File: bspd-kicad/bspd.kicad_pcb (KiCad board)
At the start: 2 copper layers, 100 x 80 mm, 113 parts, among them Q1 AO3400A, Q2 AO3401A, SW1 CJS-1200TB1, SW2 CJS-1200TB1, U5 SN74HC74DR, U6 LM1117MP-5.0, U7 SN74LVC2G14DBVR, U8 SN74LVC3G14DCUR, U9 SN74LVC3G14DCUR

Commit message: Layout Progress
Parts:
- added J1: BSPD Connector, bspd:MOLEX_430450800, F.Cu at (32.1, 125.3)
- moved C11 115.7 mm to (63.5, 141.5)
- moved R24 115.7 mm to (66.5, 139.2)
- moved R28 115.7 mm to (66.5, 143.5)
- moved TP7 115.7 mm to (66.2, 134.8)
- moved C10 115.6 mm to (57.0, 141.5)
- moved R23 115.6 mm to (60.0, 139.2)
- moved R27 115.6 mm to (60.0, 143.5)
- moved TP6 115.6 mm to (60.0, 135.0)
- moved C9 115.6 mm to (50.5, 141.2)
- moved R22 115.6 mm to (53.5, 139.2)
- moved R26 115.6 mm to (53.5, 143.5)
- moved TP5 115.6 mm to (54.0, 134.8)
- moved C8 115.5 mm to (44.0, 141.2)
- moved R21 115.5 mm to (47.0, 139.2)
- moved R25 115.5 mm to (47.0, 143.5)
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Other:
- board size 100 x 80 mm -> 79.5 x 60.8 mm
- copper layers 2 -> 4
- board text added: "FLT"
- board text added: "HB"
- board text added: "LATCH"
- board text added: "TP1"
- board text added: "TP2"
- board text added: "TPx10"

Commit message: Draft complete
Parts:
- added H1: MountingHole_Pad, MountingHole:MountingHole_3.2mm_M3_ISO14580_Pad, F.Cu at (95.0, 97.0)
- added H2: MountingHole_Pad, MountingHole:MountingHole_3.2mm_M3_ISO14580_Pad, F.Cu at (27.5, 151.0)
- added H3: MountingHole_Pad, MountingHole:MountingHole_3.2mm_M3_ISO14580_Pad, F.Cu at (27.5, 97.0)
- added H4: MountingHole_Pad, MountingHole:MountingHole_3.2mm_M3_ISO14580_Pad, F.Cu at (95.0, 151.0)
- J1: footprint bspd:MOLEX_430450800 -> bspd:MOLEX_430450600
- R29: value 47k -> 49.9k
- R30: value 56k -> 54.9k
- moved R39 15.1 mm to (44.0, 151.5), turned to 180 degrees
- moved D10 13.6 mm to (35.0, 153.5), turned to 180 degrees
- moved R11 13.5 mm to (86.0, 110.4), turned to 90 degrees
- moved R41 11.5 mm to (44.0, 149.5), turned to 180 degrees
- moved D9 11.0 mm to (48.5, 151.5), turned to 0 degrees
- moved D13 10.5 mm to (35.0, 151.5), turned to 180 degrees
- moved R40 9.63 mm to (39.5, 153.5), turned to 0 degrees
- moved D11 8.75 mm to (48.5, 149.5), turned to 0 degrees
- moved R42 8.41 mm to (44.0, 147.5), turned to 180 degrees
- moved D14 8.36 mm to (35.0, 149.5), turned to 180 degrees
- moved C16 8.28 mm to (35.5, 135.5), turned to 180 degrees
- moved D12 8.05 mm to (48.5, 147.5), turned to 0 degrees
- moved D15 7.76 mm to (35.0, 147.5), turned to 180 degrees
- moved U6 7.16 mm to (30.0, 136.0), turned to 90 degrees
- moved D5 5.88 mm to (30.0, 143.0), turned to 180 degrees
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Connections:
- R30 pad 1: Net-(Q2-G) -> +12V
- R30 pad 2: +12V -> Net-(Q2-G)
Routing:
- net Earth: track 0.00 -> 117.3 mm, vias 0 -> 183
- net HB: track 0.00 -> 100.4 mm, vias 0 -> 2
- net +12V: track 0.00 -> 87.7 mm, vias 0 -> 3
- net TPSx10%: track 0.00 -> 81.1 mm, vias 0 -> 6
- net +5V: track 0.00 -> 80.8 mm, vias 0 -> 35
- net SC_OUT: track 0.00 -> 78.1 mm, vias 0 -> 3
- net +0V45: track 0.00 -> 77.3 mm, vias 0 -> 2
- net TPS1: track 0.00 -> 73.9 mm, vias 0 -> 4
- net HB&10%: track 0.00 -> 72.8 mm, vias 0 -> 6
- net +1V25: track 0.00 -> 72.6 mm, vias 0 -> 5
- net FAULT: track 0.00 -> 70.1 mm, vias 0 -> 4
- net TPS2: track 0.00 -> 69.3 mm, vias 0 -> 4
- net BPS_FAULT: track 0.00 -> 63.3 mm, vias 0 -> 10
- net TPS2_FAULT: track 0.00 -> 61.9 mm, vias 0 -> 6
- net TPS1_FAULT: track 0.00 -> 58.2 mm, vias 0 -> 6
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- added copper zone on In2.Cu, net +5V
- added copper zone on B.Cu, net Earth
- added copper zone on F.Cu, net Earth
- added copper zone on In1.Cu, net Earth
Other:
- board size 79.5 x 60.8 mm -> 75.5 x 62 mm

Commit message: Added logos
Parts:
- added G***: LOGO, LOGO, F.Cu at (69.8, 97.5)
- added G***: LOGO, LOGO, F.Cu at (82.0, 97.5)
- added G***: LOGO, LOGO, B.Cu at (71.5, 143.2)
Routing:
- net Earth: vias 183 -> 182
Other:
- board text added: "ANUFS BSPD"
- board text added: "CG V1.0"

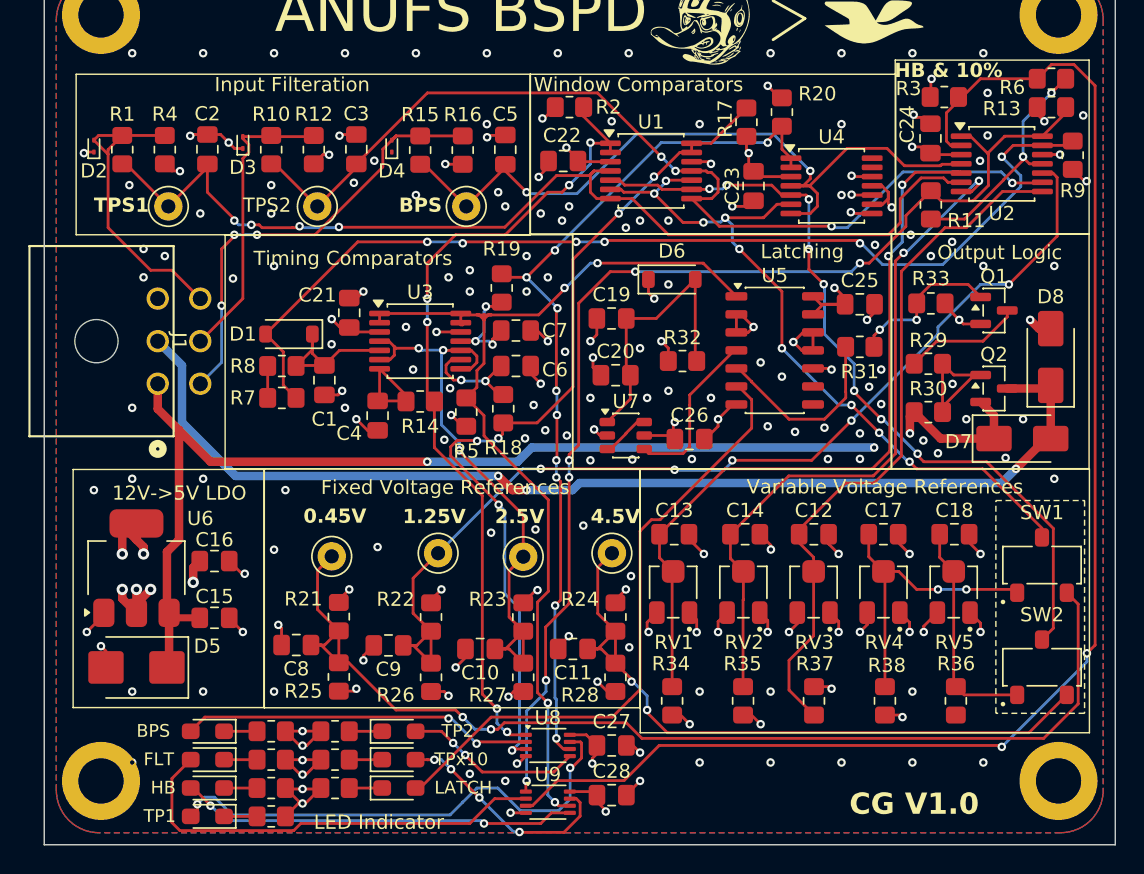
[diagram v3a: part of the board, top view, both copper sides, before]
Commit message: Moved high current line closer to connector to minimise high current trace going accross the pcb
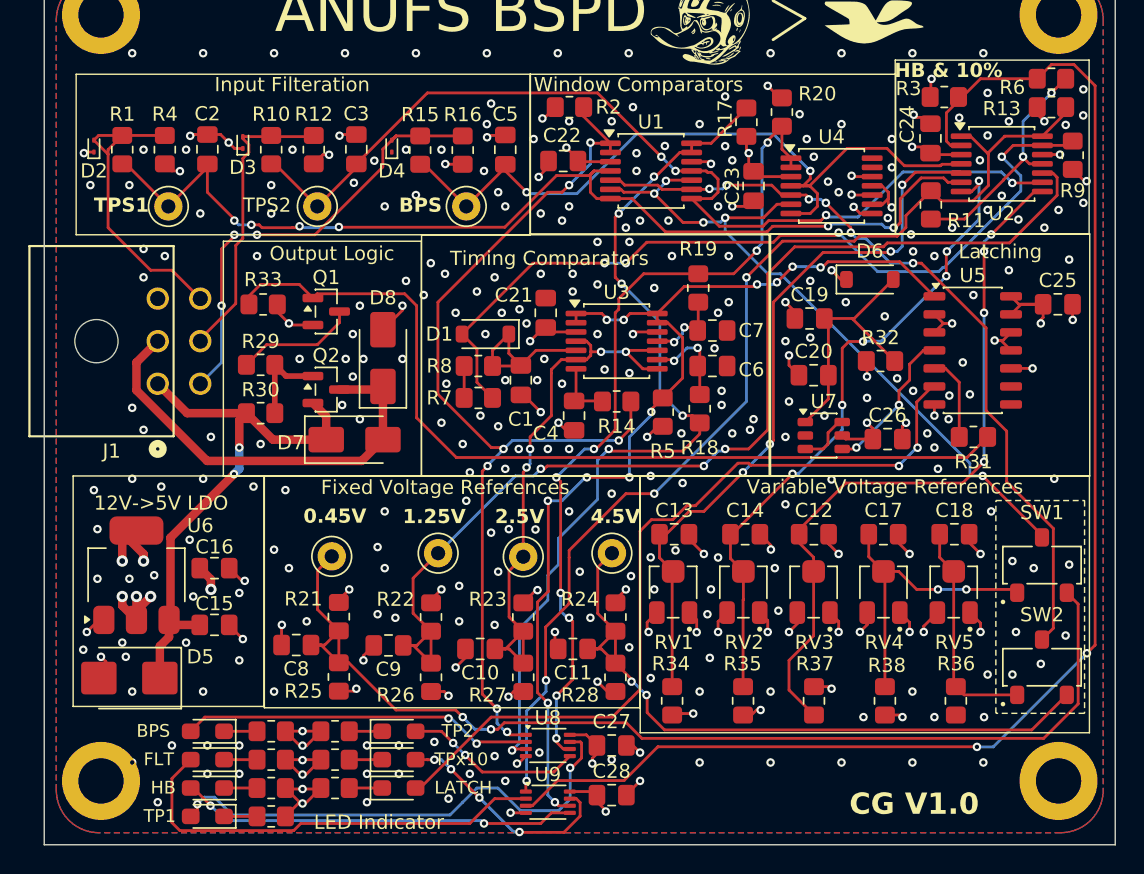
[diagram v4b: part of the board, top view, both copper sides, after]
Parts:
- moved D7 47.1 mm to (45.4, 126.9)
- moved D8 47.1 mm to (47.4, 121.2)
- moved Q1 47.1 mm to (43.4, 117.9)
- moved Q2 47.1 mm to (43.4, 123.4)
- moved R29 47.1 mm to (38.8, 121.7)
- moved R30 47.1 mm to (38.8, 125.1)
- moved R33 47.1 mm to (38.9, 117.4)
- moved C19 14.0 mm to (77.5, 118.4)
- moved C25 14.0 mm to (95.0, 117.4)
- moved C26 14.0 mm to (83.0, 126.9)
- moved D6 14.0 mm to (81.7, 115.7)
- moved R32 14.0 mm to (82.5, 121.4)
- moved U5 14.0 mm to (89.0, 120.7)
- moved U7 14.0 mm to (78.5, 126.7)
- moved C20 14.0 mm to (77.7, 122.4)
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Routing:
- net OUTPUT: track 11.1 -> 63.5 mm, vias 2 -> 0
- net +12V: track 87.7 -> 40.0 mm, vias 3 -> 2
- net SC_OUT: track 78.1 -> 31.0 mm, vias 3 -> 0
- net HB&10%: track 72.8 -> 59.7 mm, vias 6 -> 4
- net LATCH_LED: track 44.2 -> 57.0 mm, vias 0 -> 2
- net Earth: track 117.3 -> 105.3 mm, vias 182 -> 319
- net TPS1_FAULT: track 58.2 -> 68.7 mm, vias 6 -> 7
- net Net-(U5A-Q): track 13.4 -> 6.01 mm
- net TPSx10%: track 81.1 -> 76.5 mm, vias 6 -> 4
- net +1V25: track 72.6 -> 76.9 mm, vias 5 -> 3
- net Net-(Q2-G): track 10.4 -> 6.42 mm
- net BPS_FAULT: track 63.3 -> 59.8 mm, vias 10 -> 8
- net Net-(U3B-+): track 7.41 -> 4.33 mm
- net FAULT: track 70.1 -> 73.1 mm, vias 4 -> 12
- net +5V: track 80.8 -> 78.2 mm
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
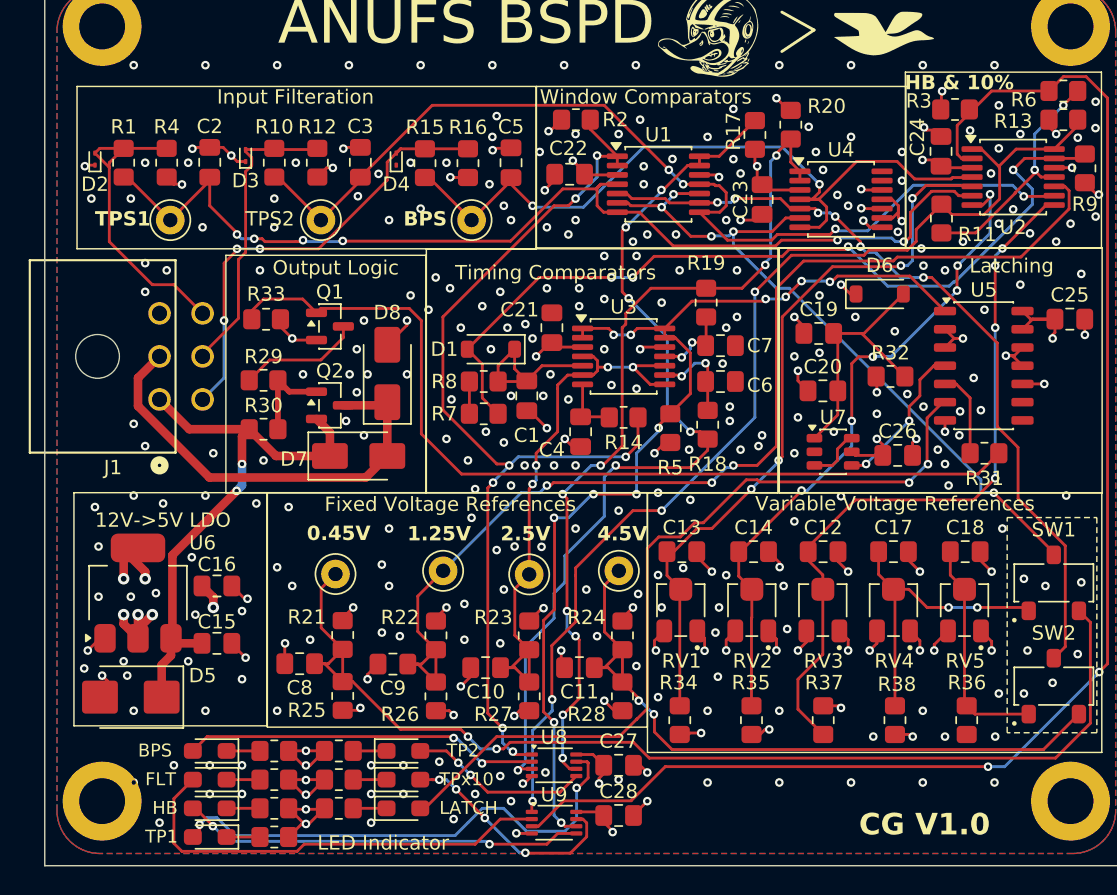
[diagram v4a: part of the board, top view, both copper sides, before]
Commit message: Footprint error, rerouting needed
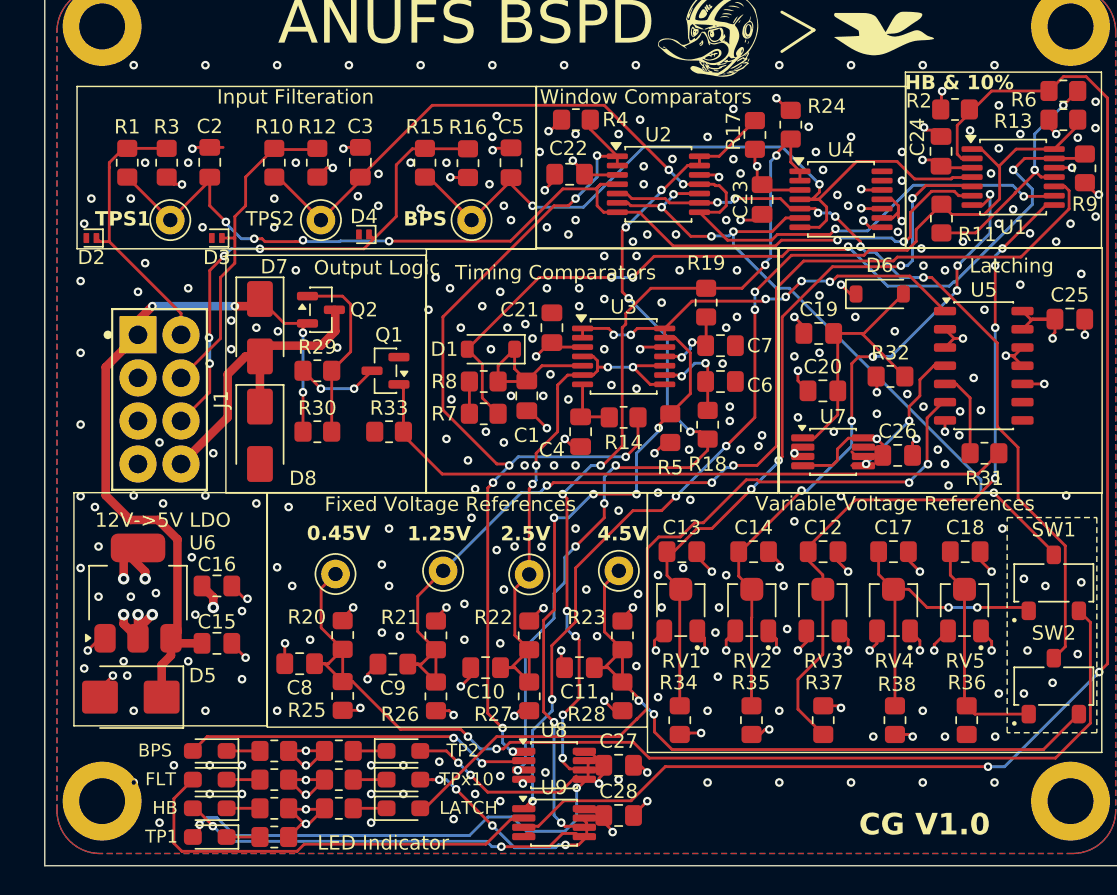
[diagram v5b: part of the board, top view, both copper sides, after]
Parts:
- D2, D3, D4: value SZESD9B5.0ST5G -> AQ1005-01ETG; footprint Diode_SMD:D_SOD-923 -> Diode_SMD:D_SOD-882
- J1: value BSPD Connector -> Conn_02x04_Counter_Clockwise; footprint bspd:MOLEX_430450600 -> bspd:WirePad_2x04_P3.0mm
- R1, R10, R15: value 10k -> 5.49k
- U7: footprint bspd:SN74LVC2G14DBVR -> Package_SO:VSSOP-8_3x3mm_P0.65mm
- U8, U9: footprint bspd:SN74LVC3G14DCUR -> Package_SO:VSSOP-8_3x3mm_P0.65mm
- moved R33 11.6 mm to (47.5, 125.2), turned to 0 degrees
- moved D7 11.3 mm to (38.5, 118.0), turned to -90 degrees
- moved D8 9.87 mm to (38.5, 125.5), turned to -90 degrees
- moved Q2 6.69 mm to (42.8, 116.8)
- moved D3 6.09 mm to (35.5, 111.8), turned to 180 degrees
- moved D4 5.71 mm to (45.8, 111.5), turned to 180 degrees
- moved D2 5.51 mm to (26.8, 111.8), turned to 180 degrees
- moved Q1 4.95 mm to (47.2, 121.0), turned to 180 degrees
- moved R29 3.81 mm to (42.5, 121.0)
- moved R30 3.75 mm to (42.5, 125.2)
- moved R1 0.25 mm to (29.2, 106.5)
- renumbered R3 to R2, R21 to R20, R22 to R21, R23 to R22, R24 to R23, R20 to R24, R4 to R3, R2 to R4, U2 to U1, U1 to U2
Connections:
- C1 pad 2: Earth -> GND
- C10 pad 2: Earth -> GND
- C11 pad 2: Earth -> GND
- C12 pad 2: Earth -> GND
- C13 pad 2: Earth -> GND
- C14 pad 2: Earth -> GND
- C15 pad 1: Earth -> GND
- C16 pad 1: Earth -> GND
- C17 pad 2: Earth -> GND
- C18 pad 2: Earth -> GND
- C19 pad 1: Earth -> GND
- C2 pad 2: Earth -> GND
- C20 pad 1: Earth -> GND
- C21 pad 2: Earth -> GND
- C22 pad 2: Earth -> GND
- C23 pad 2: Earth -> GND
- C24 pad 2: Earth -> GND
- C25 pad 2: Earth -> GND
- C26 pad 2: Earth -> GND
- C27 pad 2: Earth -> GND
- C28 pad 2: Earth -> GND
- C3 pad 2: Earth -> GND
- C4 pad 2: Earth -> GND
- C5 pad 2: Earth -> GND
- C6 pad 2: Earth -> GND
- C7 pad 2: Earth -> GND
- C8 pad 2: Earth -> GND
- C9 pad 2: Earth -> GND
- D2 pad 1: Earth -> TPS1_RAW
- D2 pad 2: TPS1_RAW -> GND
- D3 pad 1: Earth -> TPS2_RAW
- D3 pad 2: TPS2_RAW -> GND
- D4 pad 1: Earth -> BPS_RAW
- D4 pad 2: BPS_RAW -> GND
- D5 pad 2: Earth -> GND
- D8 pad 2: Earth -> GND
- H1 pad 1: Earth -> GND
- H2 pad 1: Earth -> GND
- H3 pad 1: Earth -> GND
- H4 pad 1: Earth -> GND
- J1 pad 2: SC_OUT -> unconnected-(J1-Pin_2-Pad2)
- J1 pad 3: Earth -> GND
- J1 pad 4: BPS_RAW -> GND
- J1 pad 5: TPS2_RAW -> SC_OUT
- J1 pad 6: TPS1_RAW -> BPS_RAW
- Q1 pad 2: Earth -> GND
- R12 pad 1: Earth -> GND
- R16 pad 1: Earth -> GND
- R25 pad 2: Earth -> GND
- R26 pad 2: Earth -> GND
- R27 pad 1: Earth -> GND
- R28 pad 2: Earth -> GND
- R3 pad 1: Earth -> GND
- R33 pad 1: Earth -> GND
- R34 pad 1: Earth -> GND
- R35 pad 1: Earth -> GND
- R36 pad 1: Earth -> GND
- R39 pad 2: Earth -> GND
- R40 pad 2: Earth -> GND
- R41 pad 2: Earth -> GND
- R42 pad 2: Earth -> GND
- R43 pad 2: Earth -> GND
- R44 pad 2: Earth -> GND
- R45 pad 2: Earth -> GND
- RV1 pad 3: Earth -> GND
- RV2 pad 3: Earth -> GND
- RV3 pad 3: Earth -> GND
- RV4 pad 3: Earth -> GND
- RV5 pad 3: Earth -> GND
- U1 pad 12: Earth -> GND
- U2 pad 12: Earth -> GND
- U3 pad 12: Earth -> GND
- U4 pad 10: Earth -> GND
- U4 pad 12: Earth -> GND
- U4 pad 8: Earth -> GND
- U5 pad 11: Earth -> GND
- U5 pad 12: Earth -> GND
- U5 pad 2: Earth -> GND
- U5 pad 3: Earth -> GND
- U5 pad 7: Earth -> GND
- U6 pad 1: Earth -> GND
- U7 pad 2: Earth -> GND
- U8 pad 4: Earth -> GND
- U9 pad 4: Earth -> GND
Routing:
- net Earth: track 105.3 -> 0.00 mm, vias 319 -> 0
- net GND: track 0.00 -> 97.5 mm, vias 0 -> 313
- net OUTPUT: track 63.5 -> 46.9 mm
- net +12V: track 40.0 -> 54.0 mm, vias 2 -> 4
- net SC_OUT: track 31.0 -> 21.4 mm
- net Net-(Q2-G): track 6.42 -> 12.7 mm
- net BPS_RAW: track 31.6 -> 35.5 mm, vias 3 -> 4
- net Net-(Q1-D): track 8.57 -> 5.85 mm, vias 0 -> 2
- net TPS1_RAW: track 22.0 -> 19.5 mm
- net TPS2_RAW: track 21.0 -> 22.7 mm
- net TPSx10%: vias 4 -> 6
- net TPS2_FAULT: vias 6 -> 8
- added copper zone on B.Cu, net GND
- added copper zone on F.Cu, net GND
- added copper zone on In1.Cu, net GND
- removed copper zone on B.Cu, net Earth
- removed copper zone on F.Cu, net Earth
- removed copper zone on In1.Cu, net Earth

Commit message: all issues addressed
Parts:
- U7: footprint Package_SO:VSSOP-8_3x3mm_P0.65mm -> bspd:SN74LVC2G14DBVR
- U8, U9: footprint Package_SO:VSSOP-8_3x3mm_P0.65mm -> bspd:SN74LVC3G14DCUR
- moved D5 0.35 mm to (29.5, 143.4)
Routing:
- net HB: track 99.9 -> 106.5 mm, vias 2 -> 4
- net Net-(D10-A): track 34.9 -> 33.1 mm
- net Net-(D11-A): track 15.7 -> 14.3 mm
- net FAULT: track 73.1 -> 73.9 mm
- net +0V45: track 77.3 -> 78.0 mm
- net BPS_FAULT: track 59.8 -> 60.5 mm
- net GND: track 97.5 -> 97.8 mm, vias 313 -> 329

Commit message: Move GND earth symbol into project library; complete BOM fields
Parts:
- U1, U2, U3, U4: value ~ -> TLV1704AIPWR
